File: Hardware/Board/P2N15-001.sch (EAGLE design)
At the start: 31 parts, among them IC1 TLC5941NT, IC2 LTC485N, IC3 74LS07N, IC4 LTC485N

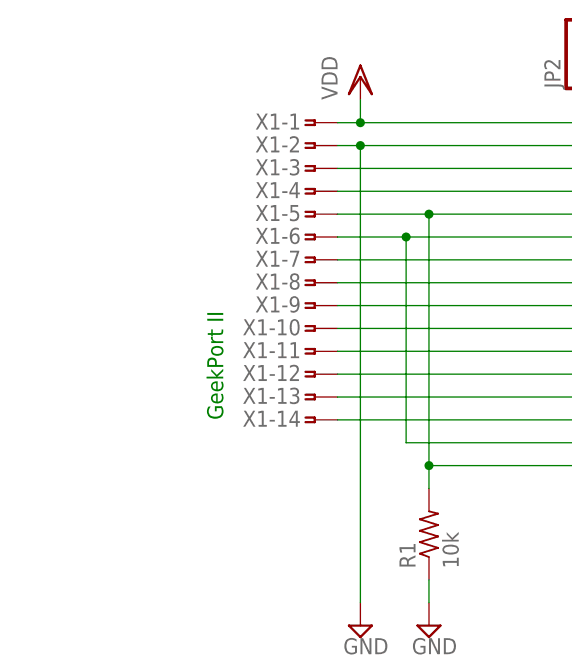
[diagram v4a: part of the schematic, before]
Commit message: Updated Hirose DX10LM1-14SE connector pattern.
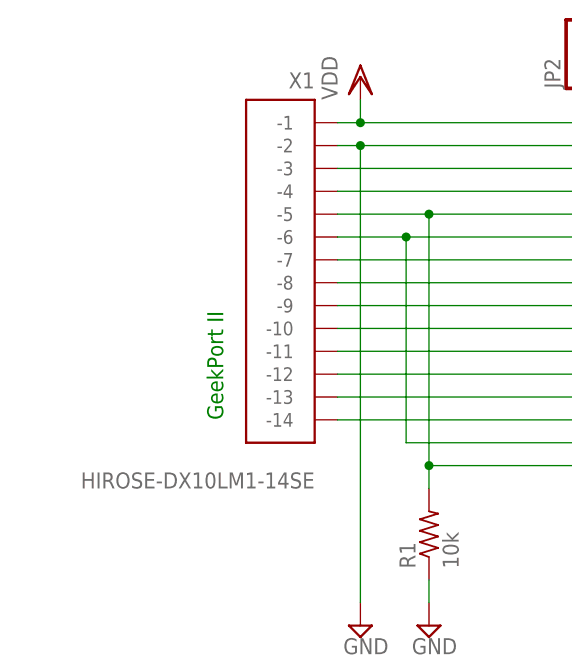
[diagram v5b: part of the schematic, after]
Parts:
- X1: value (none) -> HIROSE-DX10LM1-14SE; device con-hirose-dxlm:HIROSE-DXLM -> con-hirose-dx10lm1-14se:HIROSE-DX10LM1-14SE
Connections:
- net ANLG0: now also X1.-8; no longer X1-8.1
- net ANLG1: now also X1.-9; no longer X1-9.1
- net ANLG2: now also X1.-10; no longer X1-10.1
- net ANLG3: now also X1.-11; no longer X1-11.1
- net CD: now also X1.-6; no longer X1-6.1
- net GND: now also X1.-2; no longer X1-2.1
- net N$1: now also X1.-7; no longer X1-7.1
- net N$28: now also X1.-12; no longer X1-12.1
- net N$29: now also X1.-13; no longer X1-13.1
- net N$8: now also X1.-14; no longer X1-14.1
- net PD: now also X1.-5; no longer X1-5.1
- net USBD+: now also X1.-3; no longer X1-3.1
- net USBD-: now also X1.-4; no longer X1-4.1
- net VDD: now also X1.-1; no longer X1-1.1
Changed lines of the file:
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@@
 <part name="SUPPLY2" library="supply2" deviceset="GND" device=""/>
 <part name="SUPPLY28" library="supply2" deviceset="GND" device=""/>
-<part name="X1" library="con-hirose-dxlm" deviceset="HIROSE-DXLM" device=""/>
 <part name="VDD1" library="supply1" deviceset="VDD" device=""/>
 <part name="SUPPLY4" library="supply2" deviceset="GND" device=""/>
@@
 <part name="SUPPLY7" library="supply2" deviceset="GND" device=""/>
 <part name="R7" library="resistor" deviceset="R-US_" device="0204/5" value="220"/>
+<part name="X1" library="con-hirose-dx10lm1-14se" deviceset="HIROSE-DX10LM1-14SE" device=""/>
 </parts>
 <sheets>
@@
 <instance part="SUPPLY2" gate="GND" x="25.4" y="129.54"/>
 <instance part="SUPPLY28" gate="GND" x="297.18" y="101.6"/>
-<instance part="X1" gate="-1" x="20.32" y="185.42" rot="MR0"/>
-<instance part="X1" gate="-2" x="20.32" y="182.88" rot="MR0"/>
-<instance part="X1" gate="-3" x="20.32" y="180.34" rot="MR0"/>
-<instance part="X1" gate="-4" x="20.32" y="177.8" rot="MR0"/>
-<instance part="X1" gate="-5" x="20.32" y="175.26" rot="MR0"/>
-<instance part="X1" gate="-6" x="20.32" y="172.72" rot="MR0"/>
-<instance part="X1" gate="-7" x="20.32" y="170.18" rot="MR0"/>
-<instance part="X1" gate="-8" x="20.32" y="167.64" rot="MR0"/>
-<instance part="X1" gate="-9" x="20.32" y="165.1" rot="MR0"/>
-<instance part="X1" gate="-10" x="20.32" y="162.56" rot="MR0"/>
-<instance part="X1" gate="-11" x="20.32" y="160.02" rot="MR0"/>
-<instance part="X1" gate="-12" x="20.32" y="157.48" rot="MR0"/>
-<instance part="X1" gate="-13" x="20.32" y="154.94" rot="MR0"/>
-<instance part="X1" gate="-14" x="20.32" y="152.4" rot="MR0"/>
 <instance part="VDD1" gate="G$1" x="7.62" y="114.3"/>
 <instance part="SUPPLY4" gate="GND" x="40.64" y="93.98"/>
@@
 <instance part="SUPPLY7" gate="GND" x="104.14" y="35.56"/>
 <instance part="R7" gate="G$1" x="228.6" y="101.6"/>
+<instance part="X1" gate="G$1" x="17.78" y="154.94" rot="MR0"/>
 </instances>
 <busses>
@@
 </segment>
 <segment>
-<pinref part="X1" gate="-2" pin="1"/>
 <pinref part="SUPPLY2" gate="GND" pin="GND"/>
 <wire x1="22.86" y1="182.88" x2="25.4" y2="182.88" width="0.1524" layer="91"/>
@@
 <wire x1="83.82" y1="193.04" x2="83.82" y2="182.88" width="0.1524" layer="91"/>
 <junction x="83.82" y="182.88"/>
+<pinref part="X1" gate="G$1" pin="-2"/>
 </segment>
 <segment>
@@
 </segment>
 <segment>
-<pinref part="X1" gate="-1" pin="1"/>
 <pinref part="VDD3" gate="G$1" pin="VDD"/>
 <wire x1="22.86" y1="185.42" x2="25.4" y2="185.42" width="0.1524" layer="91"/>
@@
 <wire x1="50.8" y1="185.42" x2="50.8" y2="193.04" width="0.1524" layer="91"/>
 <junction x="25.4" y="185.42"/>
+<pinref part="X1" gate="G$1" pin="-1"/>
 </segment>
 <segment>
@@
 <net name="ANLG0" class="0">
 <segment>
-<pinref part="X1" gate="-8" pin="1"/>
 <pinref part="IC1" gate="G$1" pin="OUT1"/>
 <wire x1="22.86" y1="167.64" x2="68.58" y2="167.64" width="0.1524" layer="91"/>
@@
 <wire x1="68.58" y1="193.04" x2="68.58" y2="167.64" width="0.1524" layer="91"/>
 <junction x="68.58" y="167.64"/>
+<pinref part="X1" gate="G$1" pin="-8"/>
 </segment>
 </net>
 <net name="ANLG1" class="0">
 <segment>
-<pinref part="X1" gate="-9" pin="1"/>
 <pinref part="IC1" gate="G$1" pin="OUT2"/>
 <wire x1="22.86" y1="165.1" x2="71.12" y2="165.1" width="0.1524" layer="91"/>
@@
 <wire x1="71.12" y1="193.04" x2="71.12" y2="165.1" width="0.1524" layer="91"/>
 <junction x="71.12" y="165.1"/>
+<pinref part="X1" gate="G$1" pin="-9"/>
 </segment>
 </net>
 <net name="ANLG2" class="0">
 <segment>
-<pinref part="X1" gate="-10" pin="1"/>
 <pinref part="IC1" gate="G$1" pin="OUT3"/>
 <wire x1="22.86" y1="162.56" x2="73.66" y2="162.56" width="0.1524" layer="91"/>
@@
 <wire x1="73.66" y1="193.04" x2="73.66" y2="162.56" width="0.1524" layer="91"/>
 <junction x="73.66" y="162.56"/>
+<pinref part="X1" gate="G$1" pin="-10"/>
 </segment>
 </net>
 <net name="ANLG3" class="0">
 <segment>
-<pinref part="X1" gate="-11" pin="1"/>
 <pinref part="IC1" gate="G$1" pin="OUT4"/>
 <wire x1="22.86" y1="160.02" x2="76.2" y2="160.02" width="0.1524" layer="91"/>
@@
 <wire x1="76.2" y1="193.04" x2="76.2" y2="160.02" width="0.1524" layer="91"/>
 <junction x="76.2" y="160.02"/>
+<pinref part="X1" gate="G$1" pin="-11"/>
 </segment>
 </net>
@@
 <net name="PD" class="0">
 <segment>
-<pinref part="X1" gate="-5" pin="1"/>
 <pinref part="JP3" gate="A" pin="1"/>
 <wire x1="22.86" y1="175.26" x2="33.02" y2="175.26" width="0.1524" layer="91"/>
@@
 <wire x1="60.96" y1="193.04" x2="60.96" y2="175.26" width="0.1524" layer="91"/>
 <junction x="60.96" y="175.26"/>
+<pinref part="X1" gate="G$1" pin="-5"/>
 </segment>
 </net>
 <net name="USBD-" class="0">
 <segment>
-<pinref part="X1" gate="-4" pin="1"/>
 <pinref part="JP3" gate="A" pin="2"/>
 <wire x1="22.86" y1="177.8" x2="58.42" y2="177.8" width="0.1524" layer="91"/>
@@
 <wire x1="58.42" y1="193.04" x2="58.42" y2="177.8" width="0.1524" layer="91"/>
 <junction x="58.42" y="177.8"/>
+<pinref part="X1" gate="G$1" pin="-4"/>
 </segment>
 </net>
 <net name="USBD+" class="0">
 <segment>
-<pinref part="X1" gate="-3" pin="1"/>
 <pinref part="JP3" gate="A" pin="3"/>
 <wire x1="22.86" y1="180.34" x2="55.88" y2="180.34" width="0.1524" layer="91"/>
@@
 <wire x1="55.88" y1="193.04" x2="55.88" y2="180.34" width="0.1524" layer="91"/>
 <junction x="55.88" y="180.34"/>
+<pinref part="X1" gate="G$1" pin="-3"/>
 </segment>
 </net>
 <net name="CD" class="0">
 <segment>
-<pinref part="X1" gate="-6" pin="1"/>
 <wire x1="22.86" y1="172.72" x2="30.48" y2="172.72" width="0.1524" layer="91"/>
 <wire x1="30.48" y1="172.72" x2="30.48" y2="149.86" width="0.1524" layer="91"/>
@@
 <wire x1="63.5" y1="172.72" x2="30.48" y2="172.72" width="0.1524" layer="91"/>
 <junction x="30.48" y="172.72"/>
+<pinref part="X1" gate="G$1" pin="-6"/>
 </segment>
 </net>
 <net name="N$28" class="0">
 <segment>
-<pinref part="X1" gate="-12" pin="1"/>
 <wire x1="22.86" y1="157.48" x2="78.74" y2="157.48" width="0.1524" layer="91"/>
 <pinref part="IC1" gate="G$1" pin="OUT5"/>
@@
 <wire x1="78.74" y1="193.04" x2="78.74" y2="157.48" width="0.1524" layer="91"/>
 <junction x="78.74" y="157.48"/>
+<pinref part="X1" gate="G$1" pin="-12"/>
 </segment>
 </net>
 <net name="N$29" class="0">
 <segment>
-<pinref part="X1" gate="-13" pin="1"/>
 <wire x1="22.86" y1="154.94" x2="81.28" y2="154.94" width="0.1524" layer="91"/>
 <pinref part="IC1" gate="G$1" pin="OUT6"/>
@@
 <wire x1="81.28" y1="193.04" x2="81.28" y2="154.94" width="0.1524" layer="91"/>
 <junction x="81.28" y="154.94"/>
+<pinref part="X1" gate="G$1" pin="-13"/>
 </segment>
 </net>
@@
 <net name="N$1" class="0">
 <segment>
-<pinref part="X1" gate="-7" pin="1"/>
 <pinref part="IC1" gate="G$1" pin="OUT0"/>
 <wire x1="22.86" y1="170.18" x2="66.04" y2="170.18" width="0.1524" layer="91"/>
@@
 <wire x1="66.04" y1="193.04" x2="66.04" y2="170.18" width="0.1524" layer="91"/>
 <junction x="66.04" y="170.18"/>
+<pinref part="X1" gate="G$1" pin="-7"/>
 </segment>
 </net>
@@
 <net name="N$8" class="0">
 <segment>
-<pinref part="X1" gate="-14" pin="1"/>
 <pinref part="IC1" gate="G$1" pin="OUT7"/>
 <wire x1="22.86" y1="152.4" x2="124.46" y2="152.4" width="0.1524" layer="91"/>
 <wire x1="124.46" y1="152.4" x2="124.46" y2="144.78" width="0.1524" layer="91"/>
-</segment>
-</net>
+<pinref part="X1" gate="G$1" pin="-14"/>
+</segment>
+</net>

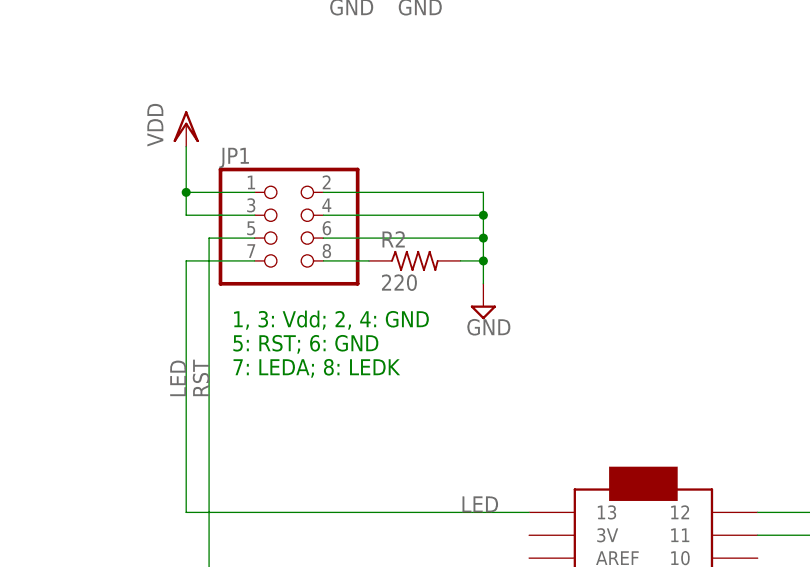
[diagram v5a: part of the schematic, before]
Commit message: Changed R value of main LED (from 220 to 150 ohm).
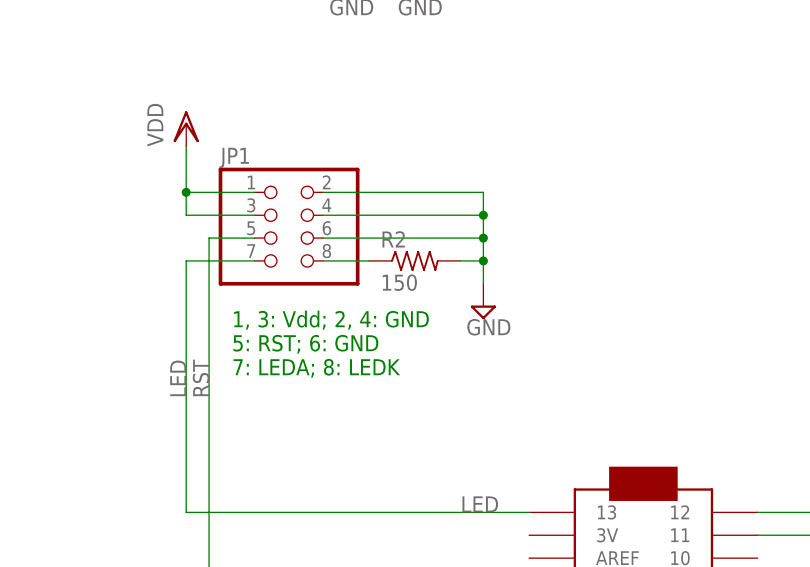
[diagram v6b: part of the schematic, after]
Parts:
- R2: value 220 -> 150
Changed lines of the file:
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@@
 <part name="VDD2" library="supply1" deviceset="VDD" device=""/>
 <part name="VDD3" library="supply1" deviceset="VDD" device=""/>
-<part name="R2" library="resistor" deviceset="R-US_" device="0204/5" value="220"/>
+<part name="R2" library="resistor" deviceset="R-US_" device="0204/5" value="150"/>
 <part name="SV1" library="con-ml" deviceset="ML10L" device=""/>
 <part name="JP3" library="pinhead" deviceset="PINHD-1X5" device="/90"/>

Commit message: Changed 10p-backport to 14p-backport.
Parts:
- added R10: 120, resistor:R-US_0204/5
- R4, R9: value 120 -> 220
- R5: value 220 -> 120
- SV1: device con-ml:ML10L -> con-ml:ML14L
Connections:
- new net N$10: R4.2, SV1.12
- net GND: now also SV1.7
- net N$15: now also R6.1; no longer R5.1
- net N$2: now also R9.1; no longer R8.1
- net N$6: now also R4.1; no longer R7.1
- net N$7: now also SV1.11; no longer SV1.7
- net RETURN: now also R9.2; no longer R8.2
- net RX+: now also R5.2; no longer R4.2
- net RX-: now also R5.1; no longer R4.1
- net RXA: now also R6.2; no longer R5.2
- net SEND: now also R8.2; no longer R6.2
- net TX+: now also R10.2; no longer R9.2
- net TX-: now also R10.1; no longer R9.1
- net VCC: now also R7.1, R8.1; no longer R6.1
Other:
- note added: "1: Contact A; 2: GND; 3: Contact B; 4: MIDI OUT Send; 5: MIDI OUT Return; 6: Vcc; 7: GND; 8: Raw TX; 9: MIDI IN Anode; 10: MIDI IN Kathode; 11: MIDI THRU Send; 12: MIDI THRU Return; 13: Sensor X; 14: Sensor Y"
- note removed: "1: Vcc; 2: GND 3: Raw TX; 4: MIDI OUT Send; 5: MIDI OUT Return 6: Contact A; 7: GND; 8: Contact B 9: MIDI IN Anode; 10: MIDI IN Kathode"
- moved on the sheet: CN1, IC3C, JP1, JP3, R1, R2, R4, R5, R6, R7, R8, R9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

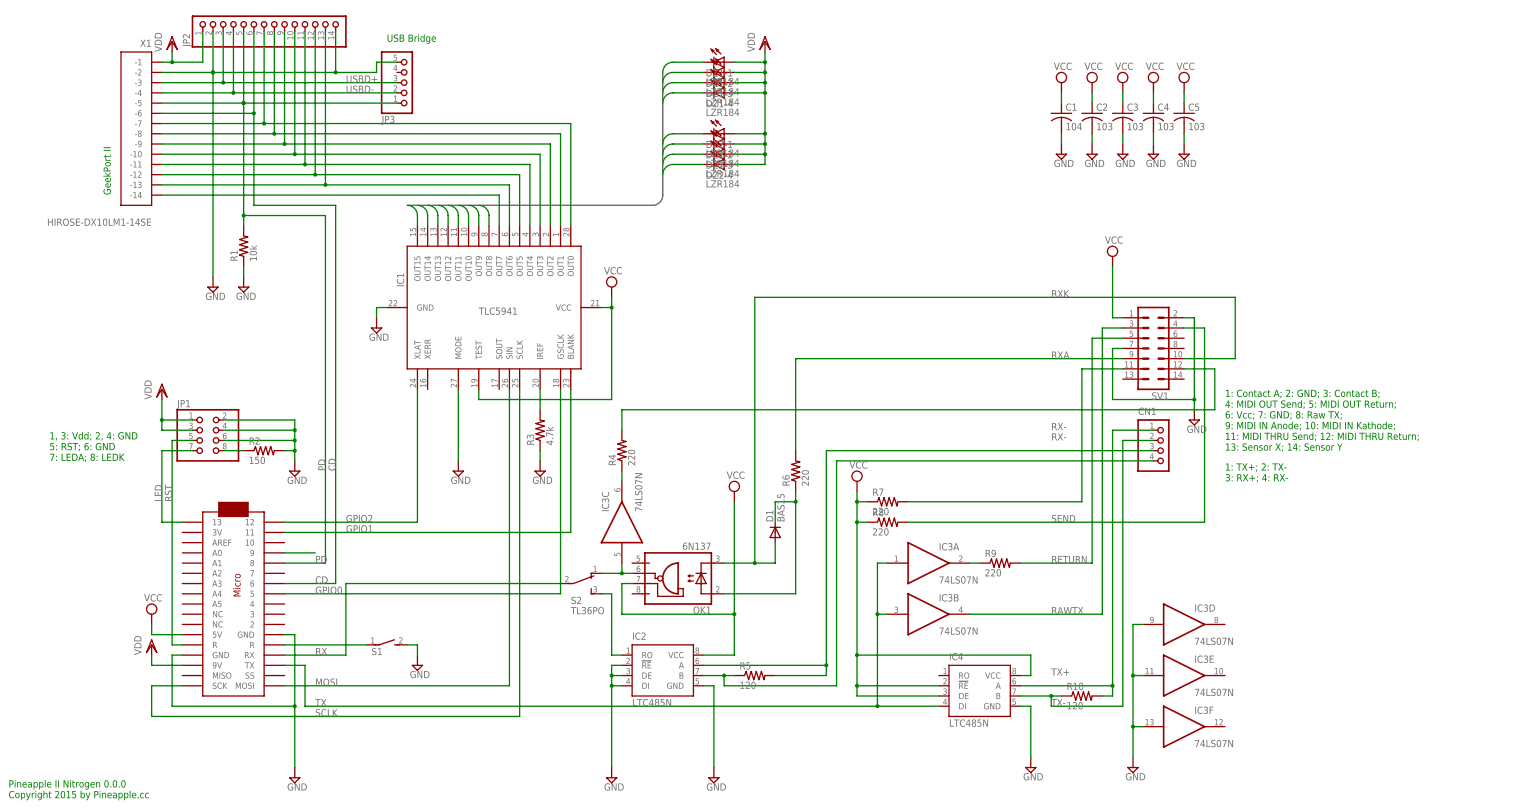
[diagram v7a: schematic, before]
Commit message: Reset of P2N15-001.{brd,sch}.
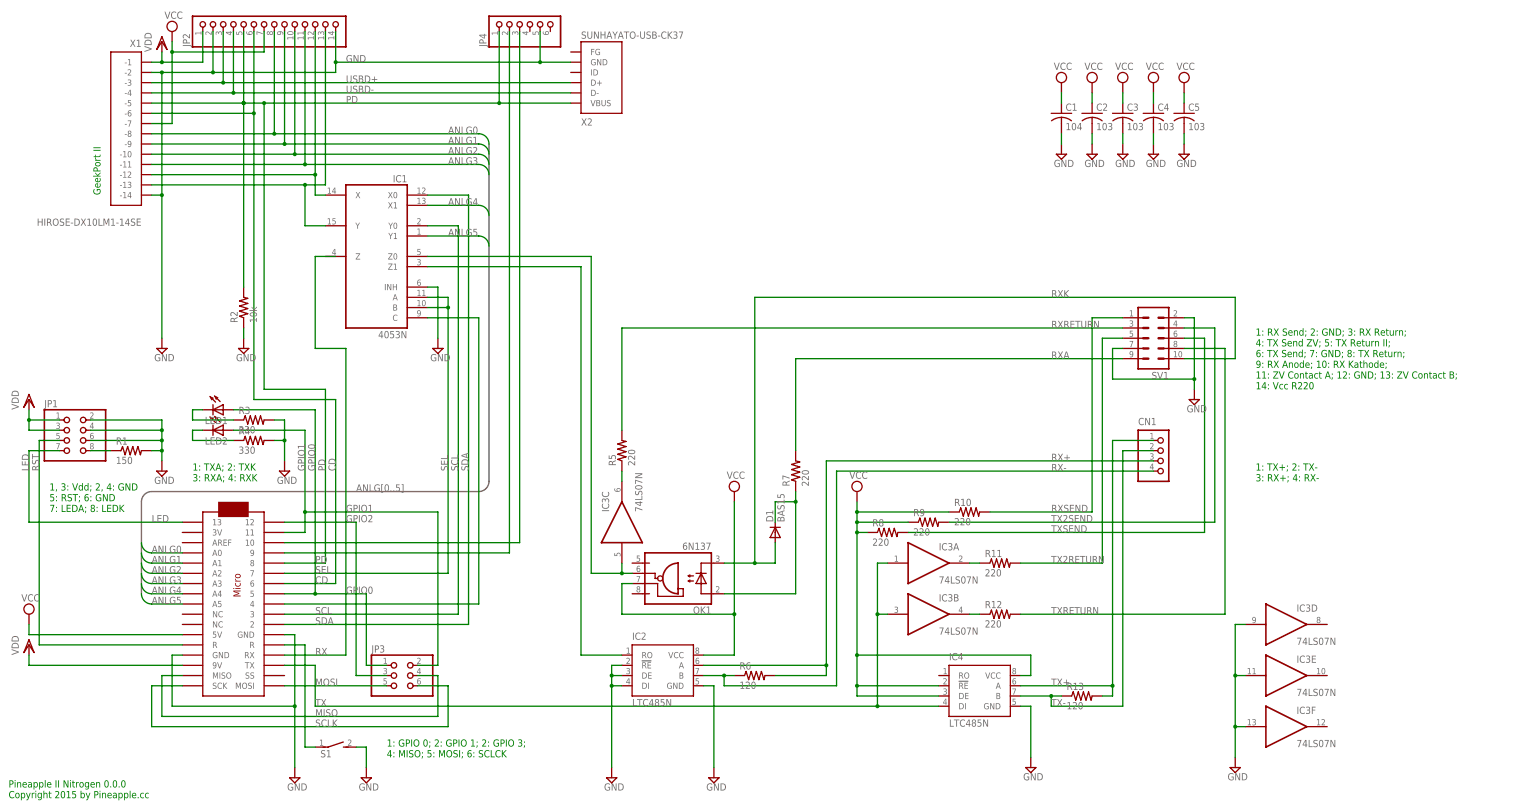
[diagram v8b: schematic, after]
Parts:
- removed DZ1, DZ2: LZR184, led:LZR184
- removed S2: TL36PO, switch:TL36PO
- added JP4: (no value), adafruit:PINHD-1X6
- added LED1, LED2: (no value), led:LED3MM
- added R11, R12: 220, resistor:R-US_0204/5
- added R13: 120, resistor:R-US_0204/5
- added X2: SUNHAYATO-USB-CK37, con-sunhayato-usb:SUNHAYATO-USB-CK37
- IC1: value TLC5941NT -> 4053N; device adafruit:TLC5941NT -> 40xx:4053N
- JP2: device pinhead:PINHD-1X14 -> adafruit:PINHD-1X14-CB
- JP3: device pinhead:PINHD-1X5/90 -> pinhead:PINHD-2X3
- R1: value 10k -> 150
- R10, R5: value 120 -> 220
- R2: value 150 -> 10k
- R3: value 4.7k -> 330
- R4: value 220 -> 330
- R6: value 220 -> 120
- SV1: device con-ml:ML14L -> con-ml:ML10L
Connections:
- removed net LED0: DZ1-1.C, IC1.OUT8
- removed net LED1: DZ1-2.C, IC1.OUT9
- removed net LED2: DZ1-3.C, IC1.OUT10
- removed net LED3: DZ1-4.C, IC1.OUT11
- removed net LED4: DZ2-1.C, IC1.OUT12
- removed net LED5: DZ2-2.C, IC1.OUT13
- removed net LED6: DZ2-3.C, IC1.OUT14
- removed net LED7: DZ2-4.C, IC1.OUT15
- removed net N$1 (its old number): IC1.OUT0, JP2.7, X1.-7
- removed net N$10: R4.2, SV1.12
- removed net N$7: R7.2, SV1.11
- removed net RAWTX: IC3B.O, SV1.3
- removed net RETURN: R9.2, SV1.5
- removed net SEND: R8.2, SV1.4
- new net ANLG4: IC1A.X1, MC1.A4
- new net ANLG5: IC1A.Y1, MC1.A5
- new net MISO: JP3.4, MC1.MISO
- new net N$17: LED1.C, R3.1
- new net N$18: LED2.C, R4.1
- new net N$5: JP4.2, MC1.9
- new net RXRETURN: R5.2, SV1.3
- new net RXSEND: R10.2, SV1.1
- new net SCL: IC1A.Y0, MC1.3
- new net SDA: IC1A.X0, MC1.2
- new net SEL: IC1A.A, IC1A.B, MC1.7
- new net TX2RETURN: R11.2, SV1.5
- new net TX2SEND: R9.2, SV1.4
- new net TXRETURN: R12.2, SV1.8
- new net TXSEND: R8.2, SV1.6
- net ANLG0: now also MC1.A0; no longer IC1.OUT1
- net ANLG1: now also MC1.A1; no longer IC1.OUT2
- net ANLG2: now also MC1.A2; no longer IC1.OUT3
- net ANLG3: now also MC1.A3; no longer IC1.OUT4
- net GND: now also IC1A.INH, JP4.5, R1.2, R2.1, R3.2, R4.2, X1.-14, X2.GND; no longer IC1.GND, IC1.MODE, JP3.5, R1.1, R2.2, R3.1
- net GPIO0: now also JP3.1, LED1.A; no longer IC1.GSCLK
- net GPIO1: now also JP3.2, LED2.A; no longer IC1.BLANK
- net GPIO2: now also JP3.3; no longer IC1.XLAT
- net MIDIRX: now also IC1A.Z0; no longer S2.O
- net MOSI: now also JP3.5; no longer IC1.SIN
- net N$15: now also R7.1; no longer R6.1
- net N$2: now also R11.1; no longer R9.1
- net N$28: now also IC1A.X; no longer IC1.OUT5
- net N$29: now also IC1A.Y; no longer IC1.OUT6
- net N$3: now also IC3C.O, R5.1; no longer MC1.9
- net N$32: now also R1.1; no longer R2.1
- net N$4: now also IC3B.O, R12.1; no longer IC1.IREF, R3.2
- net N$6: now also JP4.3, MC1.10; no longer IC3C.O, R4.1
- net N$8: now also IC1A.C, MC1.4; no longer IC1.OUT7, X1.-14
- net PD: now also JP4.1, R2.2, X2.VBUS; no longer JP3.1, R1.2
- net RX: no longer S2.P
- net RX+: now also R6.2; no longer R5.2
- net RX-: now also R6.1; no longer R5.1
- net RXA: now also R7.2; no longer R6.2
- net SCLK: now also JP3.6; no longer IC1.SCLK
- net TX+: now also R13.2; no longer R10.2
- net TX-: now also R13.1; no longer R10.1
- net USBD+: now also X2.D+; no longer JP3.3
- net USBD-: now also X2.D-; no longer JP3.2
- net VCC: now also JP2.7, R10.1, R9.1, X1.-7; no longer IC1.TEST, IC1.VCC, R7.1, SV1.1
- net VDD: no longer DZ1-1.A, DZ1-2.A, DZ1-3.A, DZ1-4.A, DZ2-1.A, DZ2-2.A, DZ2-3.A, DZ2-4.A
- net XMIDIRX: now also IC1A.Z1; no longer S2.S
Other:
- note added: "1: GPIO 0; 2: GPIO 1; 2: GPIO 3; 4: MISO; 5: MOSI; 6: SCLCK"
- note added: "1: RX Send; 2: GND; 3: RX Return; 4: TX Send ZV; 5: TX Return II; 6: TX Send; 7: GND; 8: TX Return; 9: RX Anode; 10: RX Kathode; 11: ZV Contact A; 12: GND; 13: ZV Contact B; 14: Vcc R220"
- note added: "1: TXA; 2: TXK 3: RXA; 4: RXK"
- note removed: "1: Contact A; 2: GND; 3: Contact B; 4: MIDI OUT Send; 5: MIDI OUT Return; 6: Vcc; 7: GND; 8: Raw TX; 9: MIDI IN Anode; 10: MIDI IN Kathode; 11: MIDI THRU Send; 12: MIDI THRU Return; 13: Sensor X; 14: Sensor Y"
- note removed: "USB Bridge"
- moved on the sheet: CN1, IC3D, IC3E, IC3F, JP1, R1, R10, R2, R3, R4, R5, R6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
